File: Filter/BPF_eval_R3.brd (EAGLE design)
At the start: 35.6 x 33 mm, 7 parts, among them U1 885071-A

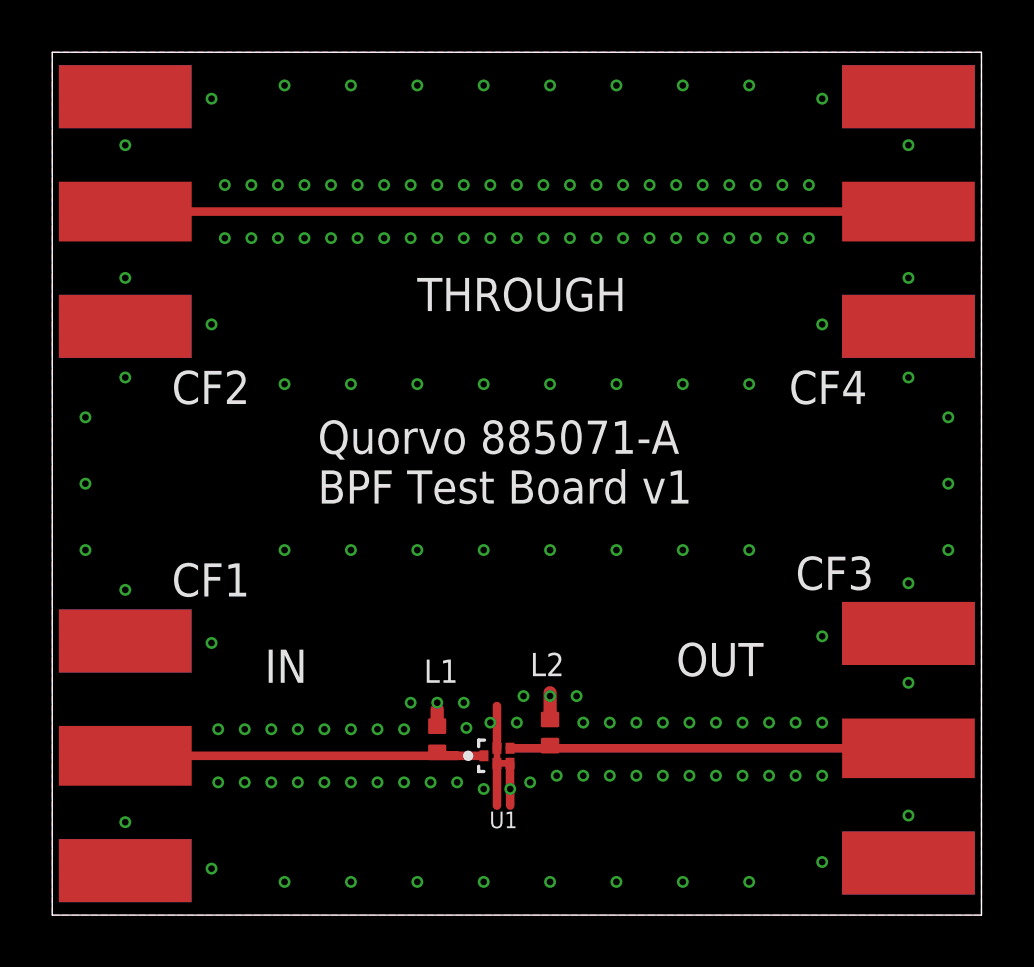
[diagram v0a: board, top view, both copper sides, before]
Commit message: Added mounting holes, cleaned up text a bit.
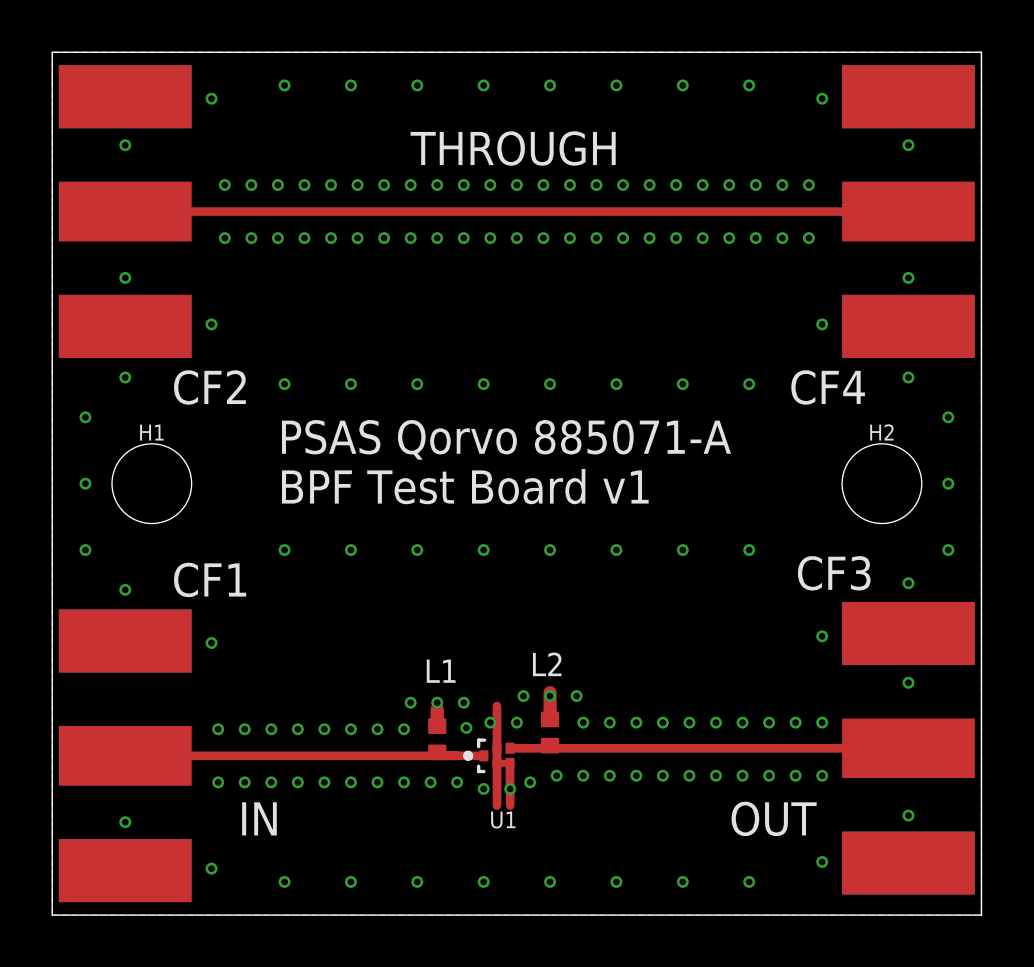
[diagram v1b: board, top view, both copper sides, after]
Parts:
- added H1, H2: STAND-OFFTIGHT, SparkFun-Hardware:STAND-OFF-TIGHT
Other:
- board text added: "PSAS Qorvo 885071-A BPF Test Board v1"
- board text removed: "Quorvo 885071-A BPF Test Board v1"
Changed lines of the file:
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@@
 <?xml version="1.0" encoding="utf-8"?>
 <!DOCTYPE eagle SYSTEM "eagle.dtd">
-<eagle version="8.5.0">
+<eagle version="8.5.1">
 <drawing>
 <settings>
@@
 <circle x="35.5092" y="6.2484" radius="0.1524" width="0.1524" layer="51"/>
 <circle x="35.5092" y="26.924" radius="0.1524" width="0.1524" layer="51"/>
-<text x="8.128" y="8.89" size="1.27" layer="21" font="vector" ratio="10">IN</text>
-<text x="23.876" y="9.144" size="1.27" layer="21" font="vector" ratio="10">OUT</text>
-<text x="13.97" y="23.114" size="1.27" layer="21" font="vector" ratio="10">THROUGH</text>
-<text x="10.16" y="15.748" size="1.27" layer="21" font="vector" ratio="10">Quorvo 885071-A
+<text x="7.112" y="3.048" size="1.27" layer="21" font="vector" ratio="10">IN</text>
+<text x="25.908" y="3.048" size="1.27" layer="21" font="vector" ratio="10">OUT</text>
+<text x="13.716" y="28.702" size="1.27" layer="21" font="vector" ratio="10">THROUGH</text>
+<text x="8.636" y="15.748" size="1.27" layer="21" font="vector" ratio="10">PSAS Qorvo 885071-A
 BPF Test Board v1</text>
 </plain>
@@
 <attribute name="NAME" x="28.194" y="19.558" size="1.27" layer="25" font="vector" ratio="20"/>
 </element>
+<element name="H1" library="SparkFun-Hardware" library_urn="urn:adsk.eagle:library:519" package="STAND-OFF-TIGHT" package3d_urn="urn:adsk.eagle:package:38629/1" value="STAND-OFFTIGHT" x="3.81" y="16.51"/>
+<element name="H2" library="SparkFun-Hardware" library_urn="urn:adsk.eagle:library:519" package="STAND-OFF-TIGHT" package3d_urn="urn:adsk.eagle:package:38629/1" value="STAND-OFFTIGHT" x="31.75" y="16.51"/>
 </elements>
 <signals>
@@
 <contactref element="CF4" pad="GND2"/>
 <via x="6.096" y="31.242" extent="1-16" drill="0.254"/>
-<wire x1="17.018" y1="6.3835" x2="17.018" y2="5.8085" width="0.254" layer="1"/>
+<wire x1="17.018" y1="6.3835" x2="17.018" y2="5.8085" width="0.3302" layer="1"/>
 <wire x1="17.018" y1="5.8085" x2="17.518" y2="5.8085" width="0.254" layer="1"/>
 <wire x1="14.732" y1="7.231" x2="14.732" y2="7.874" width="0.508" layer="1"/>
@@
 <via x="24.13" y="20.32" extent="1-16" drill="0.254"/>
 <via x="26.67" y="20.32" extent="1-16" drill="0.254"/>
-<via x="15.748" y="8.128" extent="1-16" drill="0.25"/>
-<via x="13.716" y="8.128" extent="1-16" drill="0.25"/>
-<via x="19.05" y="8.382" extent="1-16" drill="0.25"/>
-<via x="16.764" y="7.366" extent="1-16" drill="0.25"/>
-<via x="17.526" y="4.826" extent="1-16" drill="0.25"/>
+<via x="15.748" y="8.128" extent="1-16" drill="0.254"/>
+<via x="13.716" y="8.128" extent="1-16" drill="0.254"/>
+<via x="19.05" y="8.382" extent="1-16" drill="0.254"/>
+<via x="16.764" y="7.366" extent="1-16" drill="0.254"/>
+<via x="17.526" y="4.826" extent="1-16" drill="0.254"/>
 </signal>
 <signal name="THROUGH" class="1">
@@
 which will not be processed correctly with this version.
 </note>
+<note version="8.2" severity="warning">
+Since Version 8.2, EAGLE supports online libraries. The ids
+of those online libraries will not be understood (or retained)
+with this version.
+</note>
+<note version="8.3" severity="warning">
+Since Version 8.3, EAGLE supports URNs for individual library
+assets (packages, symbols, and devices). The URNs of those assets
+will not be understood (or retained) with this version.
+</note>
+<note version="8.3" severity="warning">
+Since Version 8.3, EAGLE supports the association of 3D packages
+with devices in libraries, schematics, and board files. Those 3D
+packages will not be understood (or retained) with this version.
+</note>
 </compatibility>
